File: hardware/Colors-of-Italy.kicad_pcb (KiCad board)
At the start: 2 copper layers, 178 x 178 mm, 108 parts, among them J1 Conn_01x06_Male, J10 Conn_01x03_Female, J2 JMP, J3 JMP, J4 Conn_01x03_Female, J5 Touch_Pad_+, J6 Touch_Pad_0, J7 Conn_01x03_Female, J8 Conn_01x06_Female, J9 Touch_Pad_-, P1 USB_C_Plug, Q1 2N7002, Q2 2N7002, SW1 SW_Push, SW2 SW_+_Fb, SW3 SW_0_Fb, SW4 SW_-_Fb, U1 BME280, U2 CH340G, U3 ESP32-WROOM-32, U4 AZ1117-3.3, Y1 12MHz

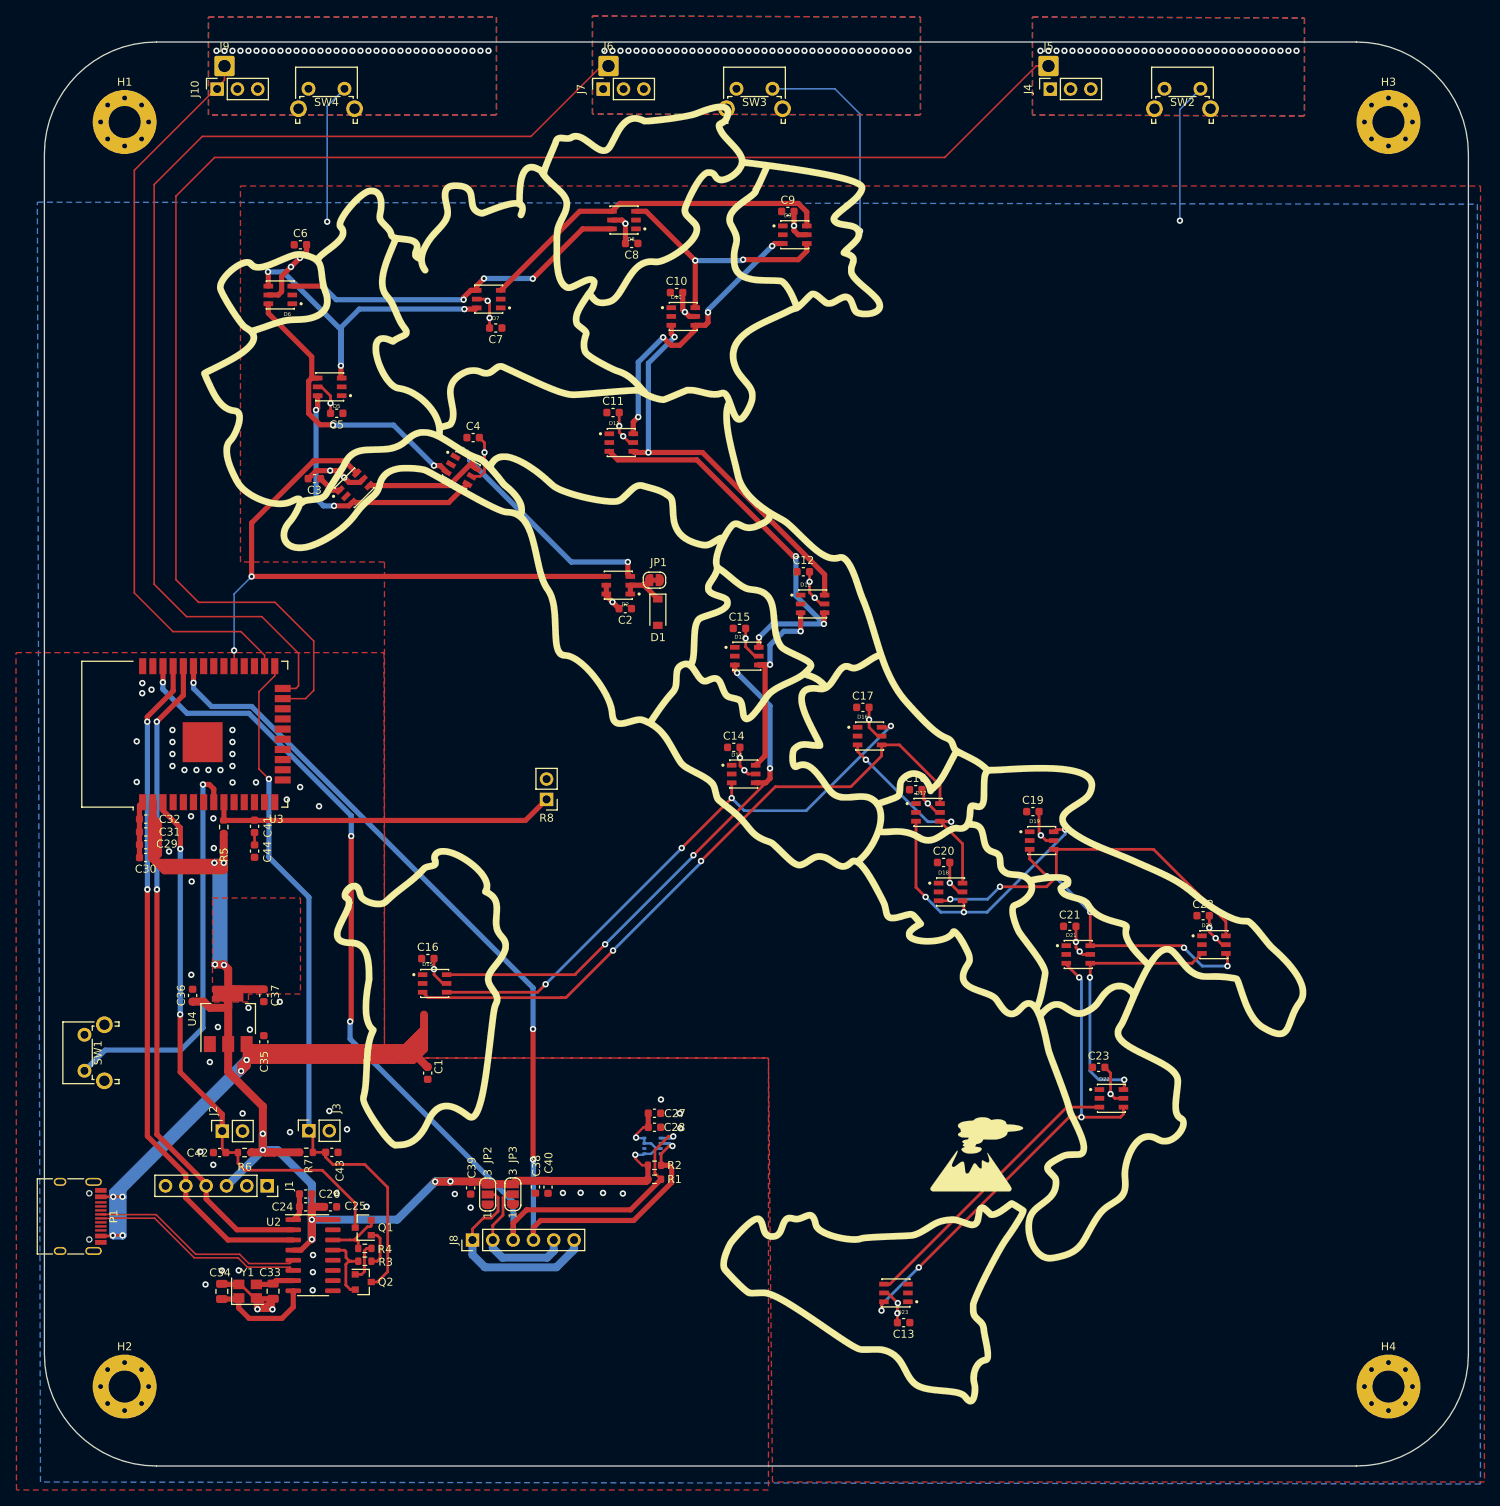
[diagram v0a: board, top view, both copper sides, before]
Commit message: fixed board outline
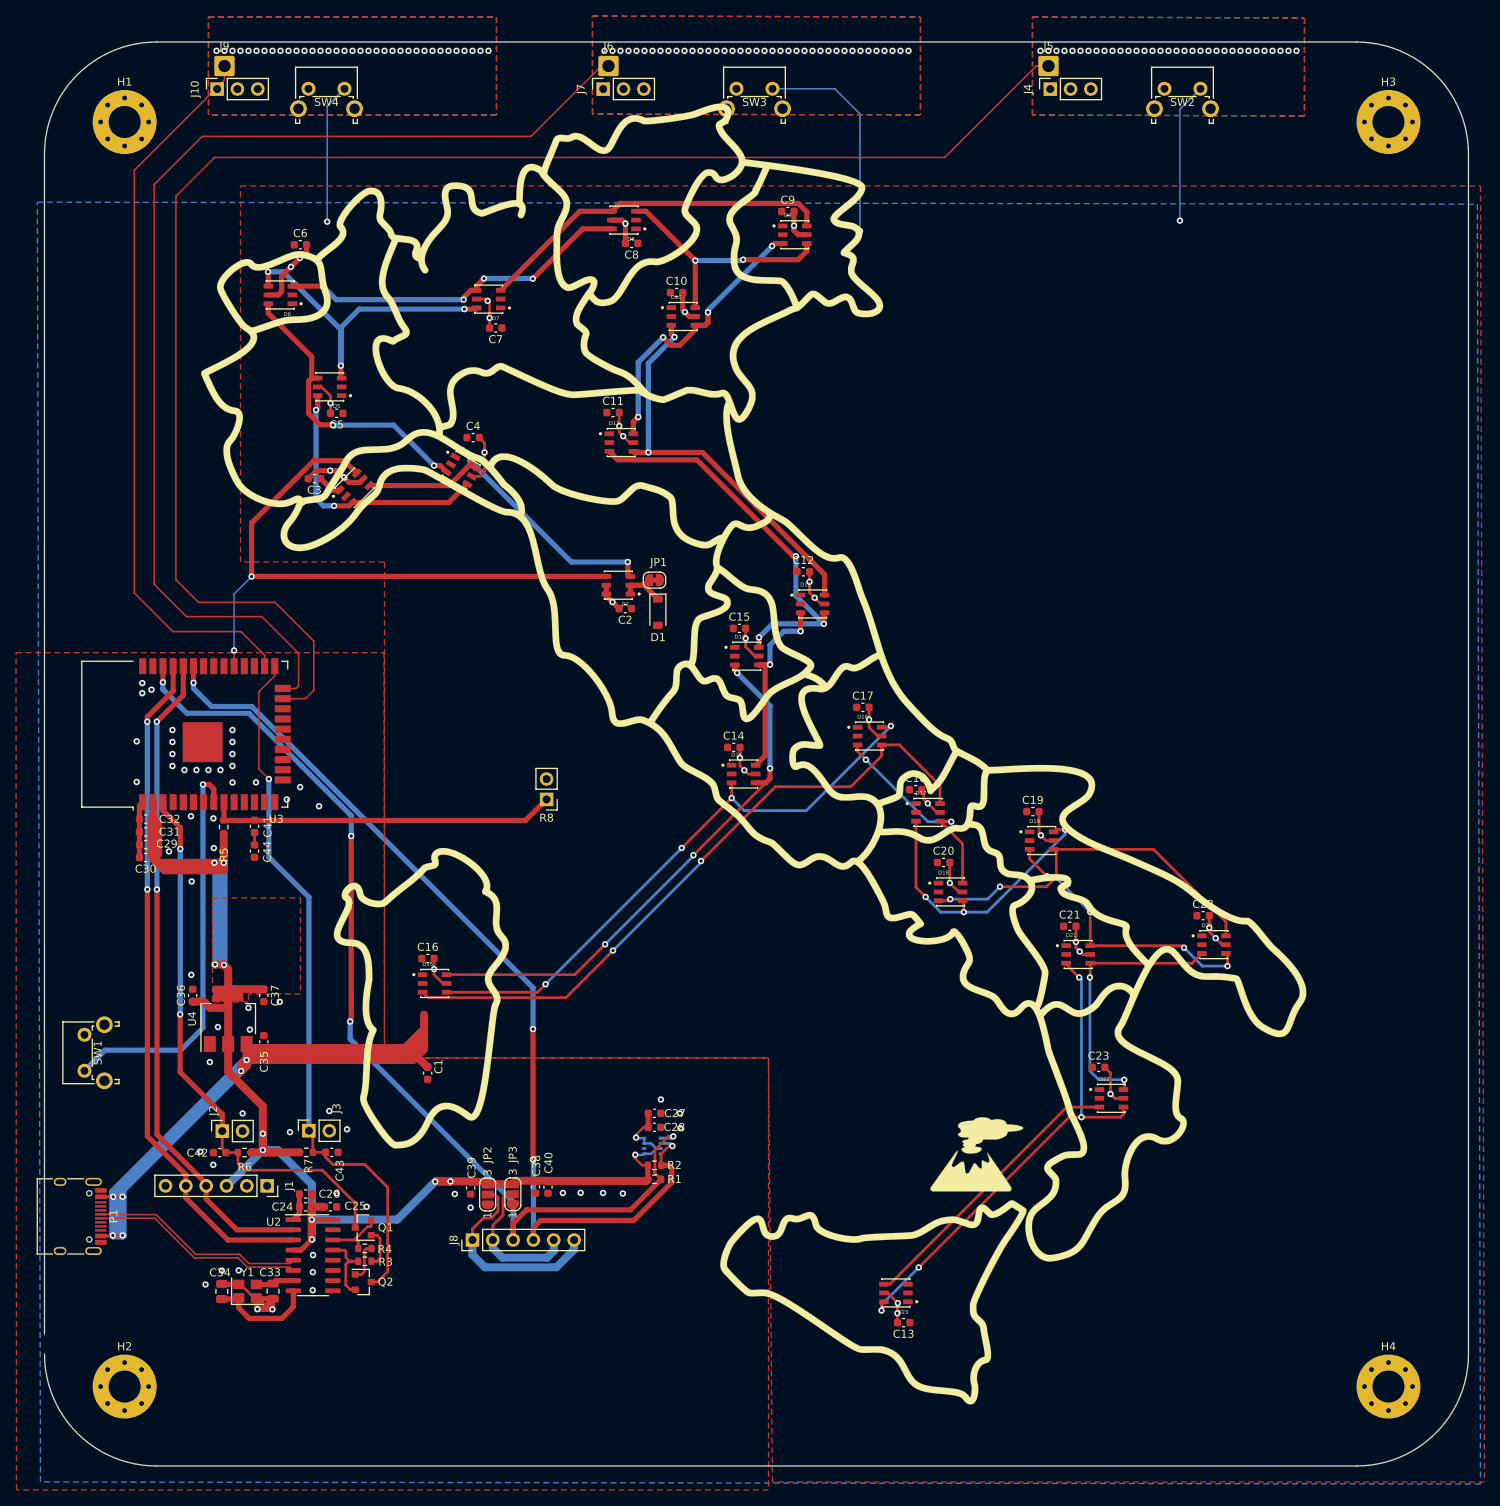
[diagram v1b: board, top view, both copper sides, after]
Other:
- outline, holes or cut-outs redrawn
